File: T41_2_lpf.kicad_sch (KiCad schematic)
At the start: 37 parts, among them J1 5-1814832-1, J2 5-1814832-1, J3 5-1814832-1, J4 Conn_02x08_Odd_Even, J5 Conn_02x05_Odd_Even, J6 B2B-XH-A_LF__SN_, Q6 Q_NMOS_GSD, U12 4002, U13 TCA9534

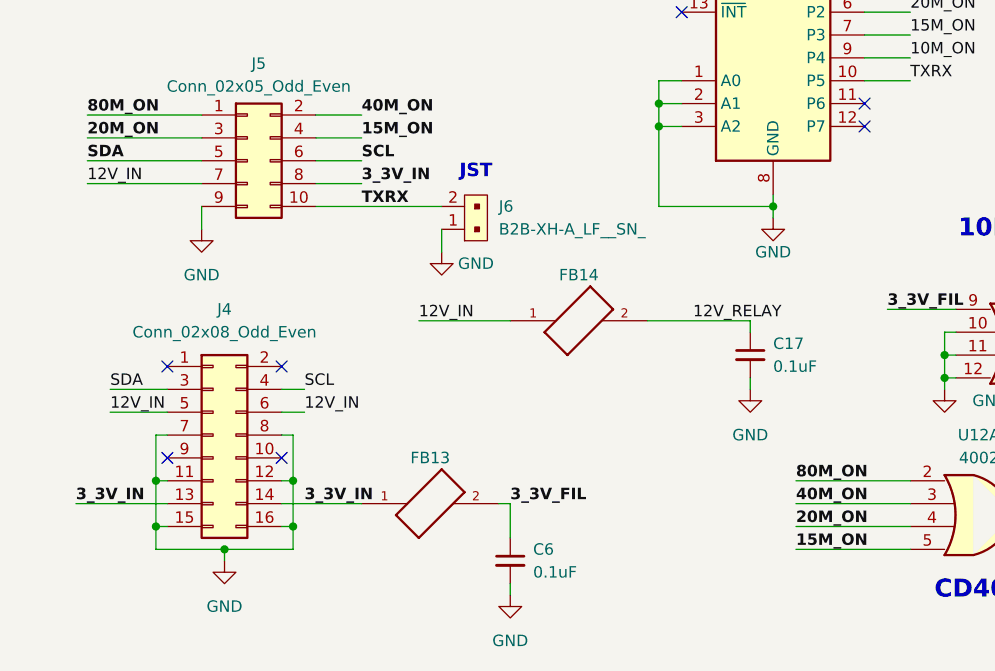
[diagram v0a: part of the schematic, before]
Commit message: Had to make minor change to accomodate V10/V11 Main Board.
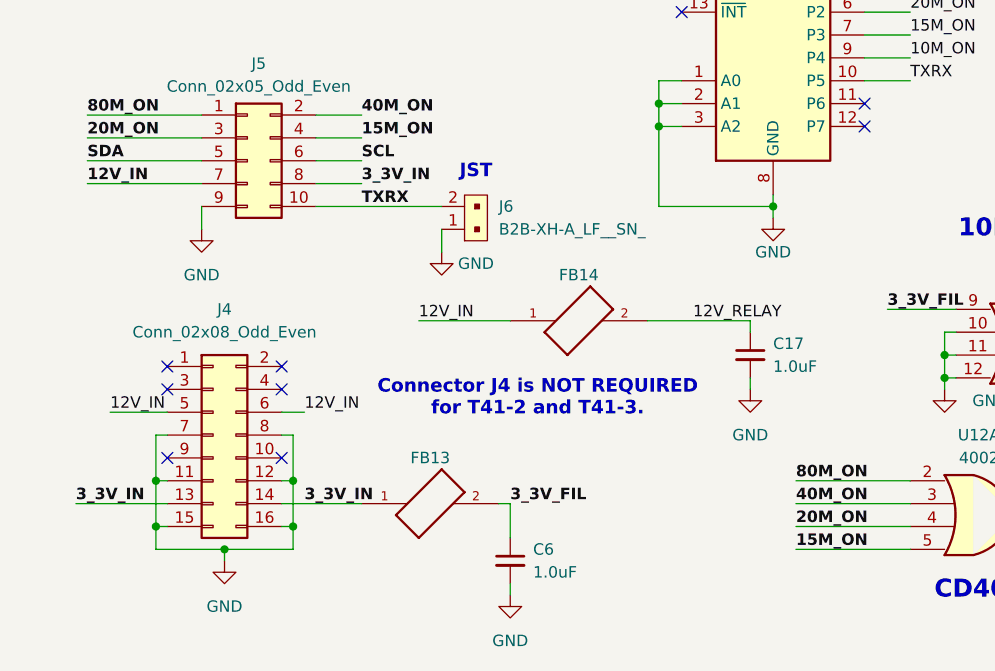
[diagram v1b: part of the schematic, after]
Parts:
- C17, C6: value 0.1uF -> 1.0uF
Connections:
- net SCL: no longer J4.4 (Pin_4)
- net SDA: no longer J4.3 (Pin_3)
- no-connect marks 38 -> 40
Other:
- note added: "Connector J4 is NOT REQUIRED for T41-2 and T41-3."
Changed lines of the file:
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@@
 		)
 	)
+	(text "Connector J4 is NOT REQUIRED\nfor T41-2 and T41-3."
+		(exclude_from_sim no)
+		(at 64.008 175.006 0)
+		(effects
+			(font
+				(size 1.5 1.5)
+				(thickness 0.254)
+				(bold yes)
+				(color 255 10 42 1)
+			)
+		)
+	)
 	(text "T41-2 LOW PASS FILTER BOARD"
 		(exclude_from_sim no)
@@
 	)
 	(no_connect
+		(at 22.86 173.99)
+	)
+	(no_connect
+		(at 35.56 173.99)
+	)
+	(no_connect
 		(at 116.84 30.48)
 	)
@@
 	(wire
 		(pts
-			(xy 35.56 173.99) (xy 38.1 173.99)
-		)
-		(stroke
-			(width 0)
-			(type default)
-		)
-	)
-	(wire
-		(pts
 			(xy 167.64 99.06) (xy 167.64 100.33)
 		)
@@
 	(wire
 		(pts
-			(xy 16.51 173.99) (xy 22.86 173.99)
-		)
-		(stroke
-			(width 0)
-			(type default)
-		)
-	)
-	(wire
-		(pts
 			(xy 100.33 129.54) (xy 105.41 129.54)
 		)
@@
 		)
 	)
-	(label "SDA"
-		(at 16.51 173.99 0)
-		(effects
-			(font
-				(size 1.27 1.27)
-			)
-			(justify left bottom)
-		)
-	)
 	(label "TXRX"
 		(at 44.45 153.67 0)
@@
 			(font
 				(size 1.27 1.27)
+				(thickness 0.254)
+				(bold yes)
 			)
 			(justify left bottom)
@@
 		)
 	)
-	(label "SCL"
-		(at 38.1 173.99 0)
-		(effects
-			(font
-				(size 1.27 1.27)
-			)
-			(justify left bottom)
-		)
-	)
 	(label "10M_ON"
 		(at 60.96 62.23 0)
@@
 			)
 		)
-		(property "Value" "0.1uF"
+		(property "Value" "1.0uF"
 			(at 90.17 171.4562 0)
 			(show_name no)
@@
 			)
 		)
-		(property "Value" "0.1uF"
+		(property "Value" "1.0uF"
 			(at 63.5 194.3162 0)
 			(show_name no)
